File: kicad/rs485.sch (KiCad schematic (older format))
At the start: 7 parts

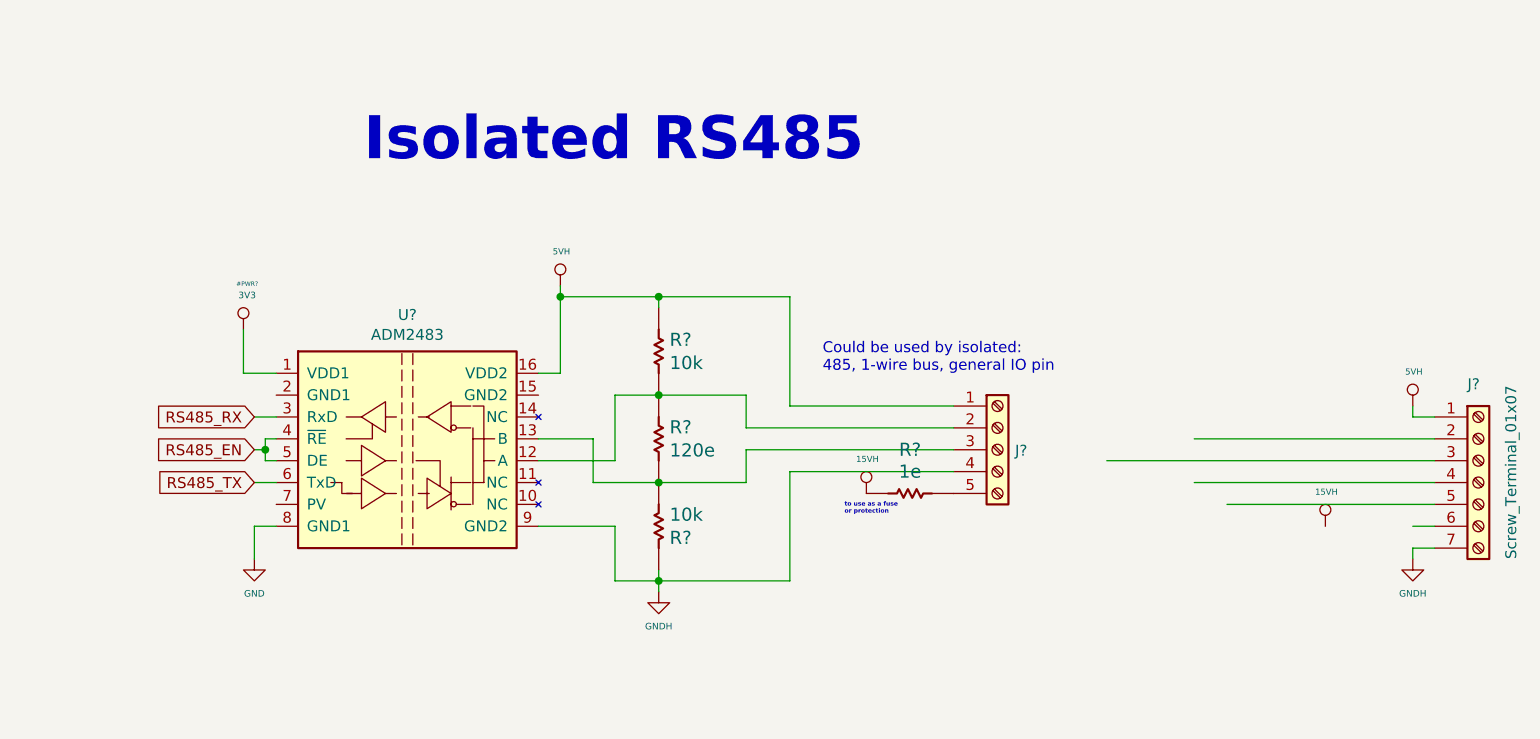
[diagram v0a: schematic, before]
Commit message: added 4 push buttons and more gpios on LCD connector
just to have more UI options. With those I'd manage graphics LCD plus 4
buttons, and charaveter LCD. or the embedded EVE graphic LCD
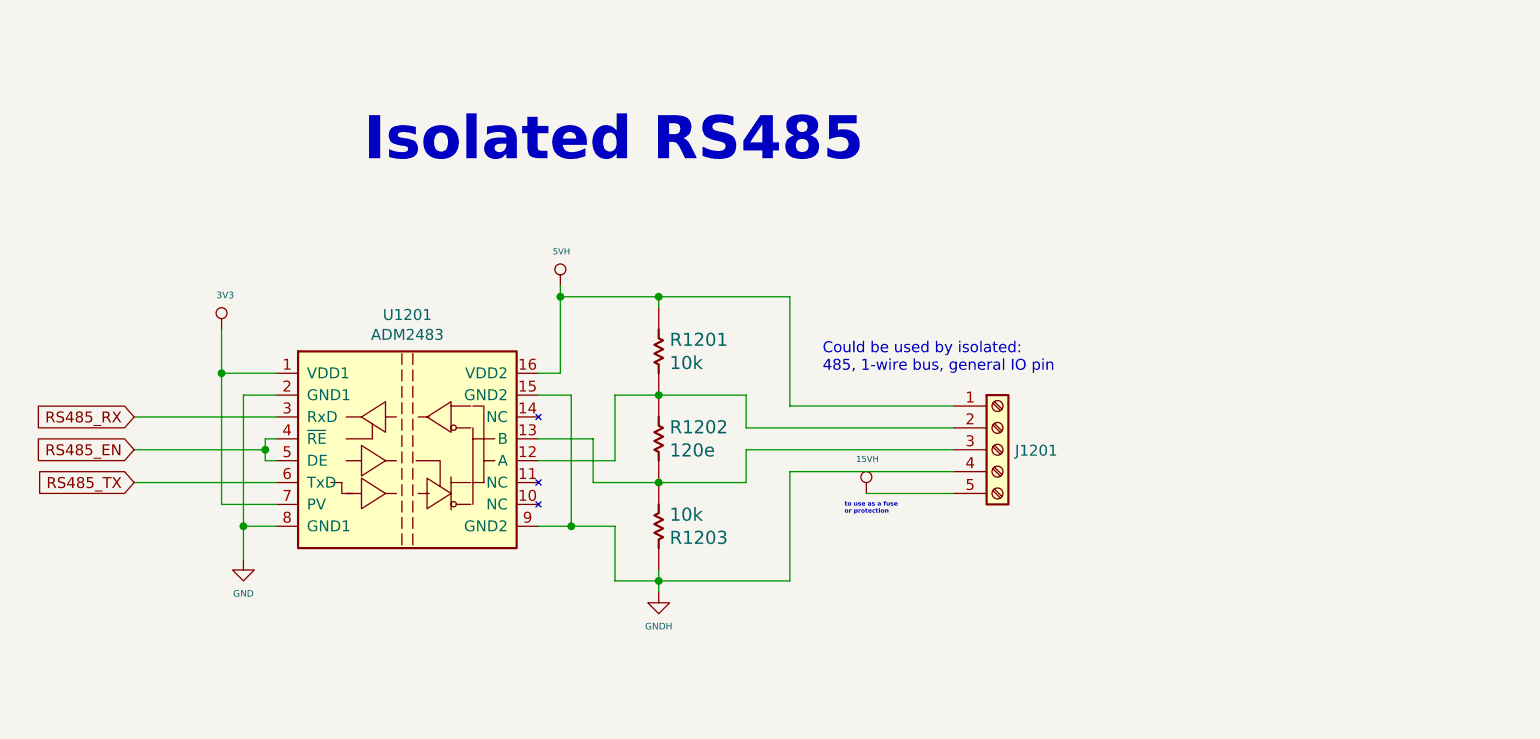
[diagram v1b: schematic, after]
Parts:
- removed J?: Screw_Terminal_01x07, symbol Connector:Screw_Terminal_01x07
- removed R?: 1e, symbol servo:Resistor
- gave numbers to parts that had none: 5
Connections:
- wire segments 48 -> 47
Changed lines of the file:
@@
 P 4500 2850
 AR Path="/5DE49152/5E1140E0" Ref="U?"  Part="1"
-AR Path="/5E1BAEAA/5E1140E0" Ref="U?"  Part="1"
-F 0 "U?" H 4500 3467 50  0000 C CNN
+AR Path="/5E1BAEAA/5E1140E0" Ref="U1201"  Part="1"
+F 0 "U1201" H 4500 3467 50  0000 C CNN
 F 1 "ADM2483" H 4500 3376 50  0000 C CNN
 F 2 "Package_SO:SOIC-16W_7.5x10.3mm_P1.27mm" H 4500 2150 50  0001 C CNN
@@
 P 5200 2100
 AR Path="/5DE49152/5E1140E7" Ref="#PWR?"  Part="1"
-AR Path="/5E1BAEAA/5E1140E7" Ref="#PWR?"  Part="1"
-F 0 "#PWR?" H 5200 1900 20  0001 C CNN
+AR Path="/5E1BAEAA/5E1140E7" Ref="#PWR0232"  Part="1"
+F 0 "#PWR0232" H 5200 1900 20  0001 C CNN
 F 1 "5VH" H 5205 2257 28  0000 C CNN
 F 2 "" H 5200 2100 50  0001 C CNN
@@
 $EndComp
 Wire Wire Line
-	3750 2500 3900 2500
-Wire Wire Line
 	5200 2150 5200 2500
 Wire Wire Line
@@
 P 5650 3500
 AR Path="/5DE49152/5E114106" Ref="#PWR?"  Part="1"
-AR Path="/5E1BAEAA/5E114106" Ref="#PWR?"  Part="1"
-F 0 "#PWR?" H 5650 3250 30  0001 C CNN
+AR Path="/5E1BAEAA/5E114106" Ref="#PWR0233"  Part="1"
+F 0 "#PWR0233" H 5650 3250 30  0001 C CNN
 F 1 "GNDH" H 5650 3342 30  0000 C CNN
 F 2 "" H 5650 3500 50  0001 C CNN
@@
 Wire Wire Line
 	5450 3200 5450 3450
-Wire Wire Line
-	3800 3200 3900 3200
 $Comp
 L servo:GND #PWR_?
 U 1 1 5E114113
-P 3800 3350
+P 3750 3350
 AR Path="/5DD4DF4C/5E114113" Ref="#PWR_?"  Part="1"
 AR Path="/5DE49152/5E114113" Ref="#PWR_?"  Part="1"
-AR Path="/5E1BAEAA/5E114113" Ref="#PWR_?"  Part="1"
-F 0 "#PWR_?" H 3805 3201 20  0001 C CNN
-F 1 "GND" H 3800 3192 30  0000 C CNN
-F 2 "" H 3800 3350 70  0000 C CNN
-F 3 "" H 3800 3350 70  0000 C CNN
-	1    3800 3350
+AR Path="/5E1BAEAA/5E114113" Ref="#PWR_0117"  Part="1"
+F 0 "#PWR_0117" H 3755 3201 20  0001 C CNN
+F 1 "GND" H 3750 3192 30  0000 C CNN
+F 2 "" H 3750 3350 70  0000 C CNN
+F 3 "" H 3750 3350 70  0000 C CNN
+	1    3750 3350
 	1    0    0    -1
 $EndComp
@@
 P 5650 2800
 AR Path="/5DE3DF56/5E11411C" Ref="R?"  Part="1"
-AR Path="/5E1BAEAA/5E11411C" Ref="R?"  Part="1"
+AR Path="/5E1BAEAA/5E11411C" Ref="R1202"  Part="1"
 AR Path="/5DE49152/5E11411C" Ref="R?"  Part="1"
-F 0 "R?" V 5597 2850 60  0000 L CNN
+F 0 "R1202" V 5597 2850 60  0000 L CNN
 F 1 "120e" V 5703 2850 60  0000 L CNN
 F 2 "" H 5650 2800 60  0000 C CNN
@@
 P 5650 3200
 AR Path="/5DE3DF56/5E114127" Ref="R?"  Part="1"
-AR Path="/5E1BAEAA/5E114127" Ref="R?"  Part="1"
+AR Path="/5E1BAEAA/5E114127" Ref="R1203"  Part="1"
 AR Path="/5DE49152/5E114127" Ref="R?"  Part="1"
-F 0 "R?" V 5597 3250 60  0000 L CNN
+F 0 "R1203" V 5597 3250 60  0000 L CNN
 F 1 "10k" V 5703 3250 60  0000 L CNN
 F 2 "" H 5650 3200 60  0000 C CNN
@@
 P 5650 2400
 AR Path="/5DE3DF56/5E11412E" Ref="R?"  Part="1"
-AR Path="/5E1BAEAA/5E11412E" Ref="R?"  Part="1"
+AR Path="/5E1BAEAA/5E11412E" Ref="R1201"  Part="1"
 AR Path="/5DE49152/5E11412E" Ref="R?"  Part="1"
-F 0 "R?" V 5597 2450 60  0000 L CNN
+F 0 "R1201" V 5597 2450 60  0000 L CNN
 F 1 "10k" V 5703 2450 60  0000 L CNN
 F 2 "" H 5650 2400 60  0000 C CNN
@@
 L servo:3V3 #PWR?
 U 1 1 5E114149
-P 3750 2300
+P 3650 2300
 AR Path="/5DCD812E/5E114149" Ref="#PWR?"  Part="1"
 AR Path="/5DD4DF4C/5E114149" Ref="#PWR?"  Part="1"
 AR Path="/5DE49152/5E114149" Ref="#PWR?"  Part="1"
-AR Path="/5E1BAEAA/5E114149" Ref="#PWR?"  Part="1"
-F 0 "#PWR?" H 3767 2509 20  0000 C CNN
-F 1 "3V3" H 3767 2457 30  0000 C CNN
-F 2 "" H 3750 2300 70  0000 C CNN
-F 3 "" H 3750 2300 70  0000 C CNN
-	1    3750 2300
+AR Path="/5E1BAEAA/5E114149" Ref="#PWR0234"  Part="1"
+F 0 "#PWR0234" H 3667 2509 20  0001 C CNN
+F 1 "3V3" H 3667 2457 30  0000 C CNN
+F 2 "" H 3650 2300 70  0000 C CNN
+F 3 "" H 3650 2300 70  0000 C CNN
+	1    3650 2300
 	1    0    0    -1
 $EndComp
@@
 	6050 2750 7000 2750
 Wire Wire Line
-	3800 3000 3900 3000
-Wire Wire Line
-	3900 2700 3800 2700
+	3250 3000 3900 3000
+Wire Wire Line
+	3900 2700 3250 2700
 Wire Wire Line
 	3900 2800 3850 2800
@@
 	3850 2900 3900 2900
 Wire Wire Line
-	3800 2850 3850 2850
+	3250 2850 3850 2850
 Connection ~ 3850 2850
 Wire Wire Line
@@
 Text Notes 6400 2500 0    50   ~ 0
 Could be used by isolated: \n485, 1-wire bus, general IO pin
-Text GLabel 3800 2850 0    50   Input ~ 0
+Text GLabel 3250 2850 0    50   Input ~ 0
 RS485_EN
-Text GLabel 3800 3000 0    50   Input ~ 0
+Text GLabel 3250 3000 0    50   Input ~ 0
 RS485_TX
-Text GLabel 3800 2700 0    50   Input ~ 0
+Text GLabel 3250 2700 0    50   Input ~ 0
 RS485_RX
 Wire Wire Line
-	3800 3200 3800 3350
+	3750 3200 3750 3350
 Wire Wire Line
 	5450 3450 5650 3450
 Wire Wire Line
-	5100 3200 5450 3200
-Wire Wire Line
-	3750 2300 3750 2500
+	5100 3200 5250 3200
+Wire Wire Line
+	3650 2300 3650 2500
 Connection ~ 5200 2150
 Text Notes 4300 1550 0    197  ~ 39
 Isolated RS485
-Wire Wire Line
-	9100 2650 9100 2700
-Wire Wire Line
-	9100 2700 9200 2700
-$Comp
-L Connector:Screw_Terminal_01x07 J?
-U 1 1 5E3395AE
-P 9400 3000
-AR Path="/5DE3DF56/5E3395AE" Ref="J?"  Part="1"
-AR Path="/5E1BAEAA/5E3395AE" Ref="J?"  Part="1"
-F 0 "J?" H 9350 3450 50  0000 L CNN
-F 1 "Screw_Terminal_01x07" V 9550 2650 50  0000 L CNN
-F 2 "" H 9400 3000 50  0001 C CNN
-F 3 "~" H 9400 3000 50  0001 C CNN
-	1    9400 3000
-	1    0    0    -1
-$EndComp
-$Comp
-L servo:5VH #PWR?
-U 1 1 5E3395B5
-P 9100 2650
-AR Path="/5DE49152/5E3395B5" Ref="#PWR?"  Part="1"
-AR Path="/5E1BAEAA/5E3395B5" Ref="#PWR?"  Part="1"
-AR Path="/5DE3DF56/5E3395B5" Ref="#PWR?"  Part="1"
-F 0 "#PWR?" H 9100 2450 20  0001 C CNN
-F 1 "5VH" H 9105 2807 28  0000 C CNN
-F 2 "" H 9100 2650 50  0001 C CNN
-F 3 "" H 9100 2650 50  0001 C CNN
-	1    9100 2650
-	1    0    0    -1
-$EndComp
-Wire Wire Line
-	7700 2900 9200 2900
-Wire Wire Line
-	8100 2800 9200 2800
-Wire Wire Line
-	8100 3000 9200 3000
-Wire Wire Line
-	9200 3100 8250 3100
-$Comp
-L servo:GNDH #PWR?
-U 1 1 5E3395BF
-P 9100 3350
-AR Path="/5DE49152/5E3395BF" Ref="#PWR?"  Part="1"
-AR Path="/5E1BAEAA/5E3395BF" Ref="#PWR?"  Part="1"
-AR Path="/5DE3DF56/5E3395BF" Ref="#PWR?"  Part="1"
-F 0 "#PWR?" H 9100 3100 30  0001 C CNN
-F 1 "GNDH" H 9100 3192 30  0000 C CNN
-F 2 "" H 9100 3350 50  0001 C CNN
-F 3 "" H 9100 3350 50  0001 C CNN
-	1    9100 3350
-	-1   0    0    -1
-$EndComp
-$Comp
-L servo:Resistor R?
-U 1 1 5E3395C5
-P 6800 3050
-AR Path="/5DE3DF56/5E3395C5" Ref="R?"  Part="1"
-AR Path="/5E1BAEAA/5E3395C5" Ref="R?"  Part="1"
-AR Path="/5DE49152/5E3395C5" Ref="R?"  Part="1"
-F 0 "R?" H 6800 2850 60  0000 C CNN
-F 1 "1e" H 6800 2950 60  0000 C CNN
-F 2 "" H 6800 3050 60  0000 C CNN
-F 3 "" H 6800 3050 60  0000 C CNN
-	1    6800 3050
-	-1   0    0    1
-$EndComp
-Wire Wire Line
-	9200 3300 9100 3300
-Wire Wire Line
-	9200 3200 9100 3200
-Wire Wire Line
-	9100 3350 9100 3300
 Text Notes 6500 3150 0    20   ~ 4
 to use as a fuse \nor protection
 $Comp
-L servo:15VH #PWR?
-U 1 1 5E3395D0
-P 8700 3200
-AR Path="/5DE3DF56/5E3395D0" Ref="#PWR?"  Part="1"
-AR Path="/5E1BAEAA/5E3395D0" Ref="#PWR?"  Part="1"
-F 0 "#PWR?" H 8700 3000 20  0001 C CNN
-F 1 "15VH" H 8705 3357 28  0000 C CNN
-F 2 "" H 8700 3200 50  0001 C CNN
-F 3 "" H 8700 3200 50  0001 C CNN
-	1    8700 3200
-	1    0    0    -1
-$EndComp
-$Comp
-L Connector:Screw_Terminal_01x05 J?
+L Connector:Screw_Terminal_01x05 J1201
 U 1 1 5E339F97
 P 7200 2850
-F 0 "J?" H 7280 2846 50  0000 L CNN
+F 0 "J1201" H 7280 2846 50  0000 L CNN
 F 1 "Screw_Terminal_01x05" H 7280 2801 50  0001 L CNN
 F 2 "" H 7200 2850 50  0001 C CNN
@@
 P 6600 3050
 AR Path="/5DE3DF56/5E33A99A" Ref="#PWR?"  Part="1"
-AR Path="/5E1BAEAA/5E33A99A" Ref="#PWR?"  Part="1"
-F 0 "#PWR?" H 6600 2850 20  0001 C CNN
+AR Path="/5E1BAEAA/5E33A99A" Ref="#PWR0238"  Part="1"
+F 0 "#PWR0238" H 6600 2850 20  0001 C CNN
 F 1 "15VH" H 6605 3207 28  0000 C CNN
 F 2 "" H 6600 3050 50  0001 C CNN
@@
 	1    0    0    -1
 $EndComp
+Wire Wire Line
+	7000 3050 6600 3050
+Wire Wire Line
+	5100 2600 5250 2600
+Wire Wire Line
+	5250 2600 5250 3200
+Connection ~ 5250 3200
+Wire Wire Line
+	5250 3200 5450 3200
+Wire Wire Line
+	3900 2600 3750 2600
+Wire Wire Line
+	3750 2600 3750 3200
+Wire Wire Line
+	3900 3100 3650 3100
+Wire Wire Line
+	3650 3100 3650 2500
+Connection ~ 3650 2500
+Wire Wire Line
+	3650 2500 3900 2500
+Connection ~ 3750 3200
+Wire Wire Line
+	3750 3200 3900 3200
 $EndSCHEMATC

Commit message: begin PCB!! it's amess but IT IS
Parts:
- R1201, R1202, R1203: footprint (none) -> Resistor_SMD:R_0603_1608Metric
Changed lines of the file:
@@
 F 0 "R1202" V 5597 2850 60  0000 L CNN
 F 1 "120e" V 5703 2850 60  0000 L CNN
-F 2 "" H 5650 2800 60  0000 C CNN
+F 2 "Resistor_SMD:R_0603_1608Metric" H 5650 2800 60  0000 C CNN
 F 3 "" H 5650 2800 60  0000 C CNN
 	1    5650 2800
@@
 F 0 "R1203" V 5597 3250 60  0000 L CNN
 F 1 "10k" V 5703 3250 60  0000 L CNN
-F 2 "" H 5650 3200 60  0000 C CNN
+F 2 "Resistor_SMD:R_0603_1608Metric" H 5650 3200 60  0000 C CNN
 F 3 "" H 5650 3200 60  0000 C CNN
 	1    5650 3200
@@
 F 0 "R1201" V 5597 2450 60  0000 L CNN
 F 1 "10k" V 5703 2450 60  0000 L CNN
-F 2 "" H 5650 2400 60  0000 C CNN
+F 2 "Resistor_SMD:R_0603_1608Metric" H 5650 2400 60  0000 C CNN
 F 3 "" H 5650 2400 60  0000 C CNN
 	1    5650 2400

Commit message: I've passed all footprin to layout BUT...
I've passed all, first glance... I need to confirm in details a lot of
things. The objetive for these is to have an aproximation of the size
I'll need to make the board.. then I choose the final detailed footprint
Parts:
- removed J1201: Screw_Terminal_01x05, symbol Connector:Screw_Terminal_01x05
- added J1201: tblock, TerminalBlock_RND:TerminalBlock_RND_205-00289_1x04_P5.08mm_Horizontal, symbol Connector:Screw_Terminal_01x04
- added JP1201: Jumper_3_Bridged12, Jumper:SolderJumper-3_P1.3mm_Open_RoundedPad1.0x1.5mm, symbol servo:Jumper_3_Bridged12
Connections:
- net 15VH: now also JP1201.3 (B)
- net 5VH: now also JP1201.1 (A)
- net GNDH: now also R1203.2, J1201.4 (Pin_4); no longer R1203.1
- net at R1201.2, R1202.1, U1201.12 (A): now also J1201.2 (Pin_2)
- net at R1202.2, U1201.13 (B): now also R1203.1, J1201.3 (Pin_3); no longer R1203.2
- new net: J1201.1 (Pin_1), JP1201.2 (C)
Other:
- note added: "With these interfase you could manage isolated RS485 or isolated \n GPIO or isolated 1-Wire, using 5H or 15H as a supply"
- note removed: "to use as a fuse \nor protection"
- moved on the sheet: R1201, R1202, R1203, U1201
